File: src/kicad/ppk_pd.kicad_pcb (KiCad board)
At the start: 2 copper layers, 30 x 20 mm, 24 parts

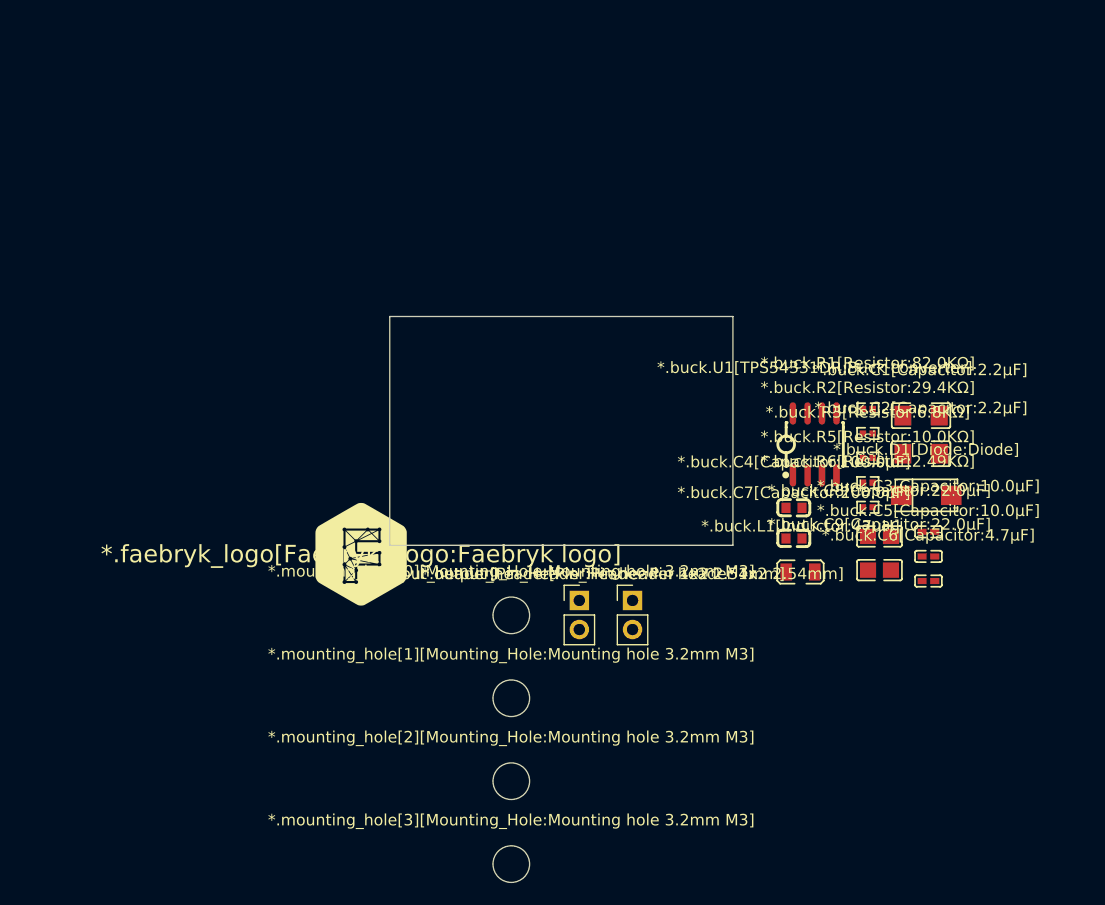
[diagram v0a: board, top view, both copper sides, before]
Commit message: Add jlcpcb_db function that executes the SQL queries and handles the database
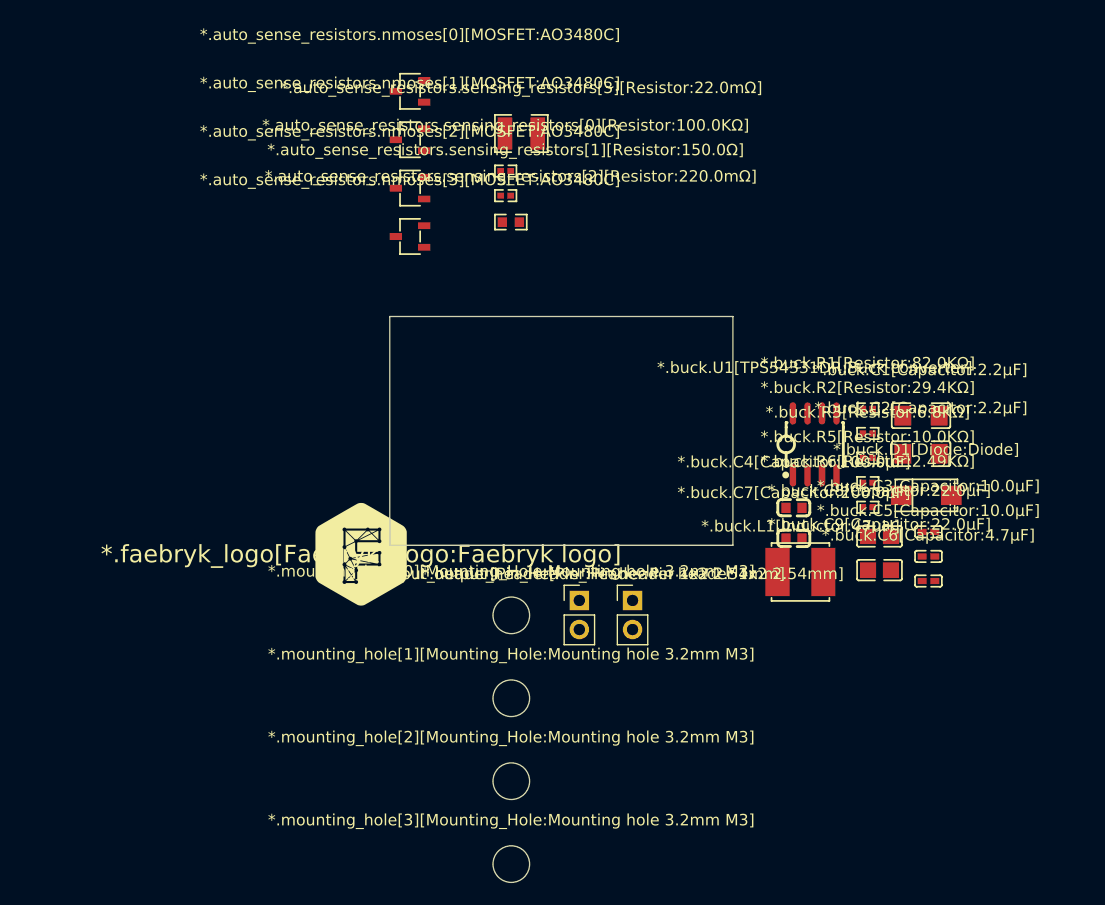
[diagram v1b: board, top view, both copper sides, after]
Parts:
- added *.auto_sense_resistors.nmoses[0][MOSFET:AO3480C]: AO3480C, lcsc:SOT-23-3_L2.9-W1.6-P1.90-LS2.8-BR, F.Cu at (48.8, 8.31)
- added *.auto_sense_resistors.nmoses[1][MOSFET:AO3480C]: AO3480C, lcsc:SOT-23-3_L2.9-W1.6-P1.90-LS2.8-BR, F.Cu at (48.8, 12.5)
- added *.auto_sense_resistors.nmoses[2][MOSFET:AO3480C]: AO3480C, lcsc:SOT-23-3_L2.9-W1.6-P1.90-LS2.8-BR, F.Cu at (48.8, 16.8)
- added *.auto_sense_resistors.nmoses[3][MOSFET:AO3480C]: AO3480C, lcsc:SOT-23-3_L2.9-W1.6-P1.90-LS2.8-BR, F.Cu at (48.8, 21.0)
- added *.auto_sense_resistors.sensing_resistors[0][Resistor:100.0KΩ]: 100.0KΩ, lcsc:R0402, F.Cu at (57.1, 15.3)
- added *.auto_sense_resistors.sensing_resistors[1][Resistor:150.0Ω]: 150.0Ω, lcsc:R0402, F.Cu at (57.1, 17.4)
- added *.auto_sense_resistors.sensing_resistors[2][Resistor:220.0mΩ]: 220.0mΩ, lcsc:R0603, F.Cu at (57.6, 19.7)
- added *.auto_sense_resistors.sensing_resistors[3][Resistor:22.0mΩ]: 22.0mΩ, lcsc:R1210, F.Cu at (58.5, 12.0)
- *.buck.L1[Inductor:47uH]: footprint lcsc:IND-SMD_L2.5-W2.0-A -> lcsc:IND-SMD_L5.0-W5.0
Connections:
- net *.buck.C1[Capacitor:2.2µF]-*.buck.C3[Capacitor:10.0µF]-*.buck.R1[Resistor:82.0KΩ]-*.buck.C2[Capacitor:2.2µF]-*.buck.U1[TPS54331DR:Buck converter] renamed *.buck.C1[Capacitor:2.2µF]-*.buck.R1[Resistor:82.0KΩ]-*.buck.C3[Capacitor:10.0µF]-*.buck.U1[TPS54331DR:Buck converter]-*.buck.C2[Capacitor:2.2µF]
- net *.buck.C6[Capacitor:4.7µF]-*.buck.C7[Capacitor:200.0µF]-*.buck.U1[TPS54331DR:Buck converter] renamed *.buck.C7[Capacitor:200.0µF]-*.buck.U1[TPS54331DR:Buck converter]-*.buck.C6[Capacitor:4.7µF]
- net *.buck.C9[Capacitor:22.0µF]-*.buck.D1[Diode:Diode]-*.buck.U1[TPS54331DR:Buck converter]-*.buck.R2[Resistor:29.4KΩ]-*.buck.C1[Capacitor:2.2µF]-*.buck.C3[Capacitor:10.0µF]-*.buck.C2[Capacitor:2.2µF]-*.buck.C5[Capacitor:10.0µF]-*.buck.C7[Capacitor:200.0µF]-*.buck.R3[Resistor:6.8KΩ]-*.buck.R6[Resistor:2.49KΩ]-*.buck.C8[Capacitor:22.0µF] renamed *.buck.R2[Resistor:29.4KΩ]-*.buck.R6[Resistor:2.49KΩ]-*.buck.C1[Capacitor:2.2µF]-*.buck.C3[Capacitor:10.0µF]-*.buck.C7[Capacitor:200.0µF]-*.buck.D1[Diode:Diode]-*.buck.C5[Capacitor:10.0µF]-*.buck.R3[Resistor:6.8KΩ]-*.buck.U1[TPS54331DR:Buck converter]-*.buck.C8[Capacitor:22.0µF]-*.buck.C9[Capacitor:22.0µF]-*.buck.C2[Capacitor:2.2µF]
- net *.buck.D1[Diode:Diode]-*.buck.U1[TPS54331DR:Buck converter]-*.buck.L1[Inductor:47uH]-*.buck.C4[Capacitor:100.0µF] renamed *.buck.C4[Capacitor:100.0µF]-*.buck.U1[TPS54331DR:Buck converter]-*.buck.D1[Diode:Diode]-*.buck.L1[Inductor:47uH]
- net *.buck.R1[Resistor:82.0KΩ]-*.buck.R2[Resistor:29.4KΩ]-*.buck.U1[TPS54331DR:Buck converter] renamed *.buck.R2[Resistor:29.4KΩ]-*.buck.U1[TPS54331DR:Buck converter]-*.buck.R1[Resistor:82.0KΩ]
- net *.buck.R5[Resistor:10.0KΩ]-*.buck.L1[Inductor:47uH]-*.buck.C8[Capacitor:22.0µF]-*.buck.C9[Capacitor:22.0µF] renamed *.buck.C9[Capacitor:22.0µF]-*.buck.R5[Resistor:10.0KΩ]-*.buck.C8[Capacitor:22.0µF]-*.buck.L1[Inductor:47uH]
